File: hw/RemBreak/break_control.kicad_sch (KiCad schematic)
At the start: 13 parts, among them J6 Conn_01x07, J7 Conn_01x07, J8 Conn_01x03, Q10 BC337, Q11 BC847

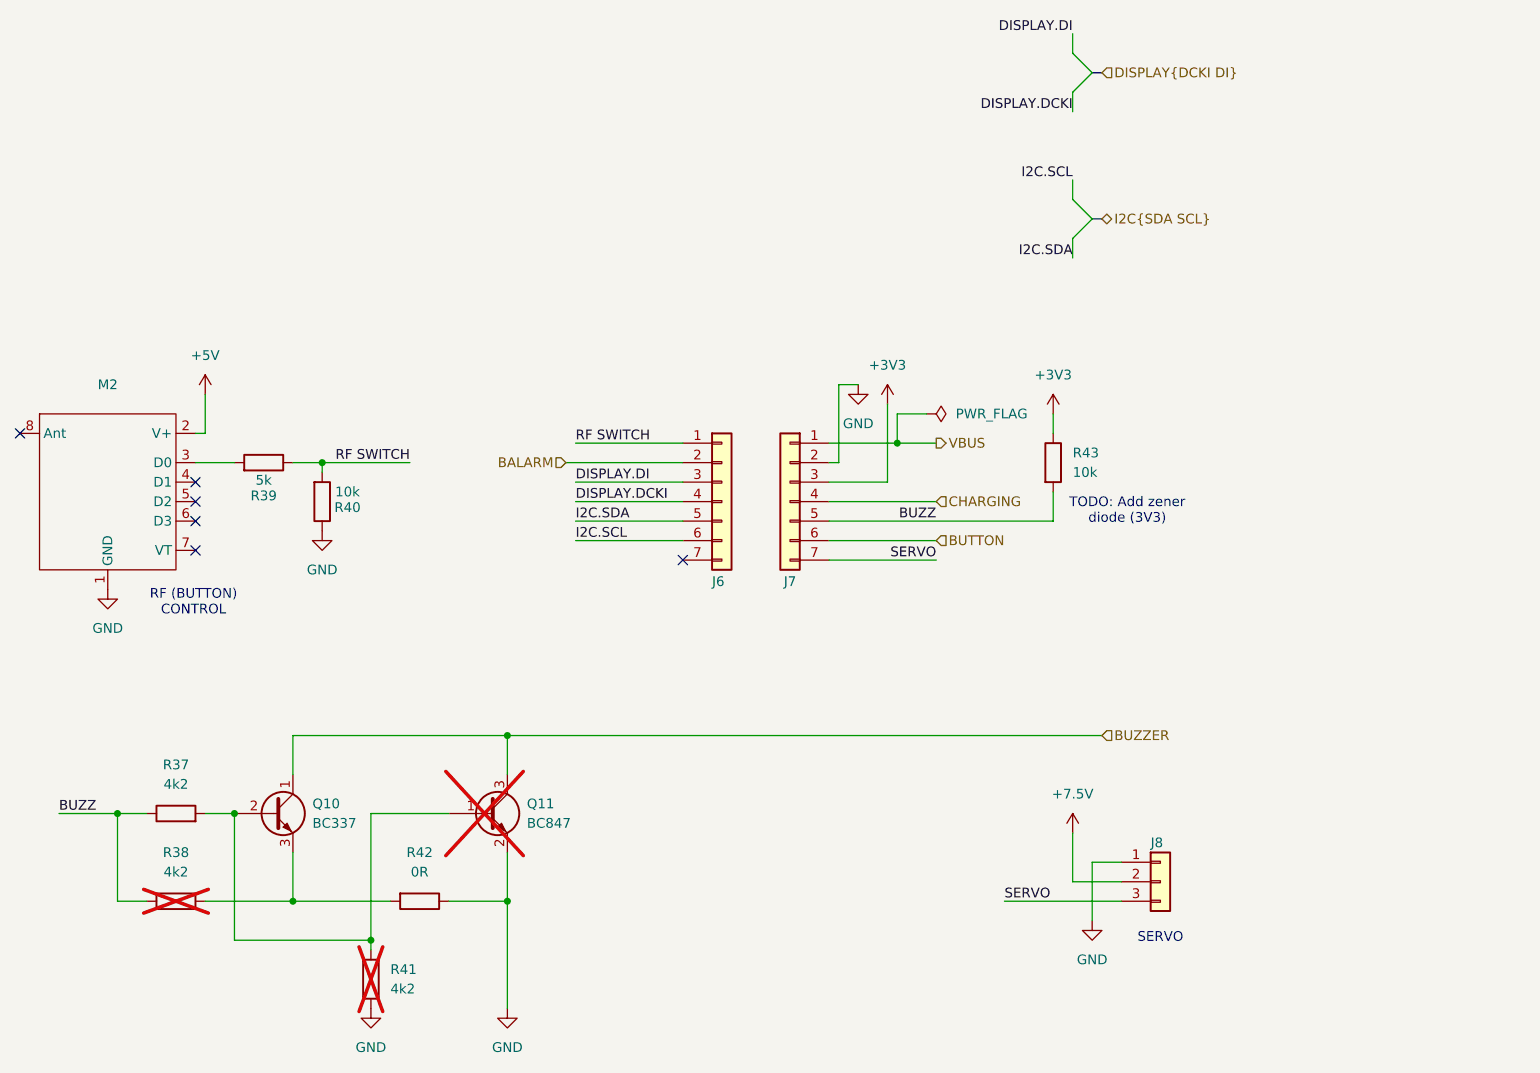
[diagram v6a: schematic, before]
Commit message: Note fonts changed to bold and added titles of the sheets included rev number
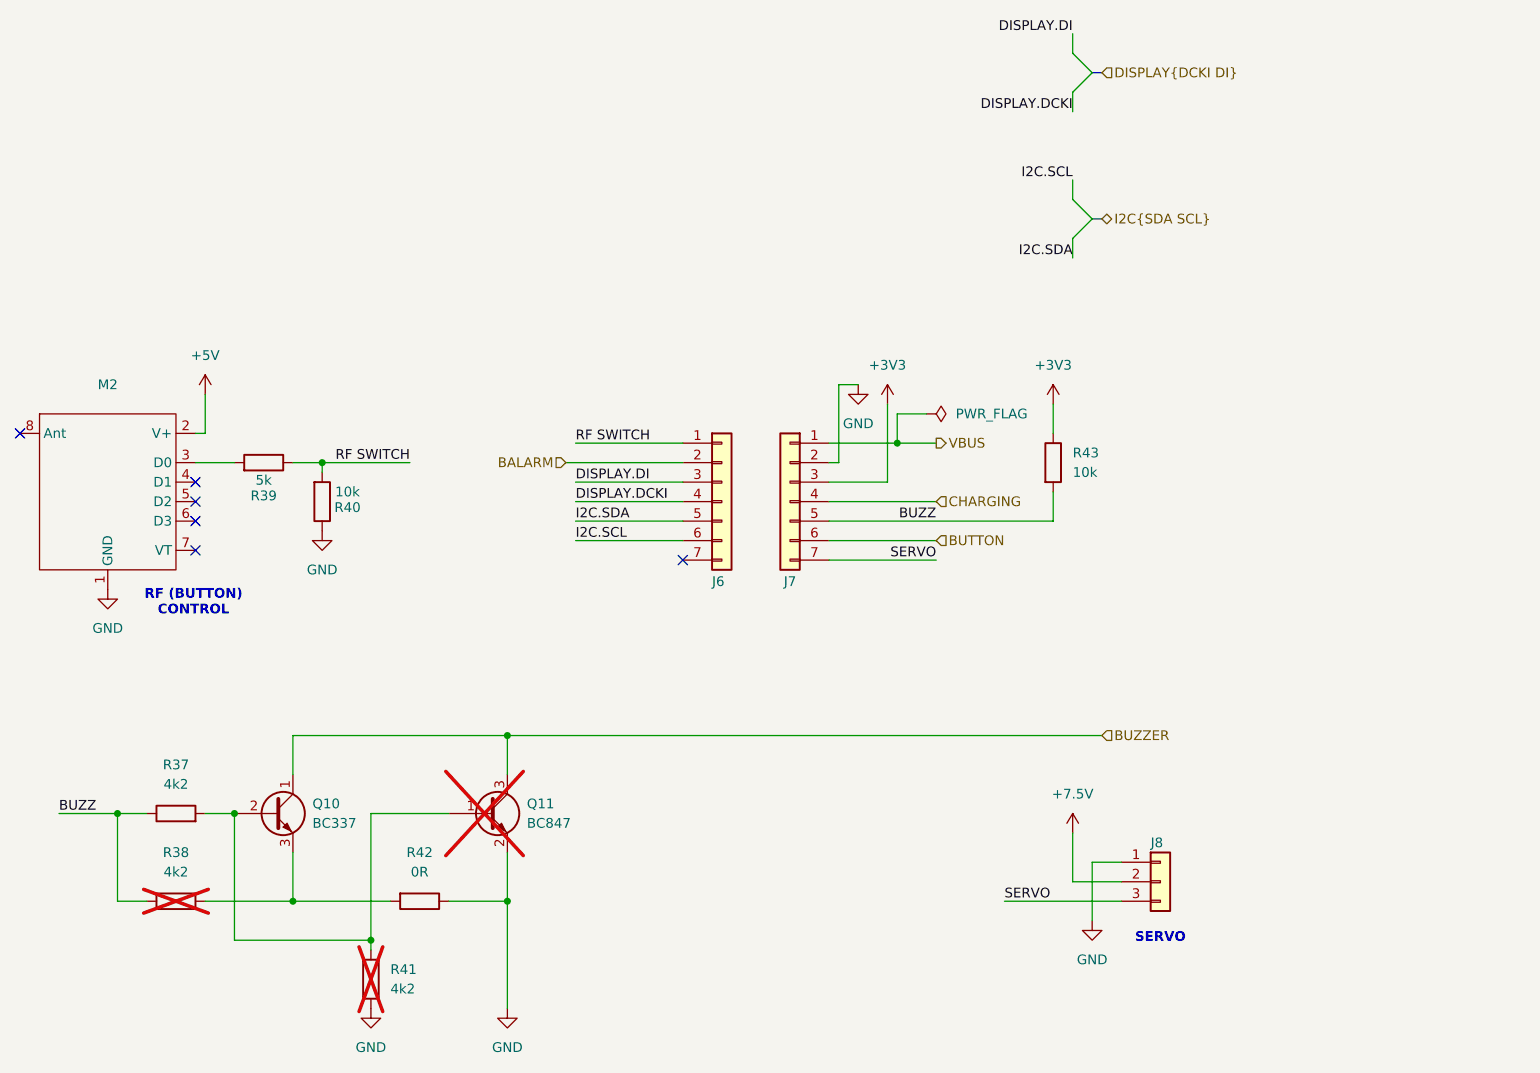
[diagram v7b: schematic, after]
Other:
- note removed: "TODO: Add zener diode (3V3)"
- title: (none) -> Break Control
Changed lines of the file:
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@@
 	(generator_version "8.99")
 	(paper "A4")
+	(title_block
+		(title "Break Control")
+		(date "2024-12-15")
+		(rev "1.0")
+	)
 	(bus_alias "DISPLAY"
 		(members "DISP_DI" "DISP_DCKI")
@@
 			(font
 				(size 1.27 1.27)
-			)
-		)
-	)
-	(text "TODO: Add zener \ndiode (3V3)"
-		(exclude_from_sim no)
-		(at 198.882 95.25 0)
-		(effects
-			(font
-				(size 1.27 1.27)
-				(color 255 0 0 1)
+				(thickness 0.254)
+				(bold yes)
 			)
 		)
@@
 			(font
 				(size 1.27 1.27)
+				(thickness 0.254)
+				(bold yes)
 			)
 		)
@@
 	(wire
 		(pts
-			(xy 189.23 82.55) (xy 189.23 85.09)
+			(xy 189.23 81.28) (xy 189.23 85.09)
 		)
 		(stroke
@@
 	(symbol
 		(lib_id "power:+3V3")
-		(at 189.23 82.55 0)
+		(at 189.23 81.28 0)
 		(unit 1)
 		(exclude_from_sim no)
@@
 		(fields_autoplaced yes)
 		(property "Reference" "#PWR045"
-			(at 189.23 86.36 0)
+			(at 189.23 85.09 0)
 			(effects
 				(font
@@
 		)
 		(property "Value" "+3V3"
-			(at 189.23 77.47 0)
+			(at 189.23 76.2 0)
 			(effects
 				(font
@@
 		)
 		(property "Footprint" ""
-			(at 189.23 82.55 0)
+			(at 189.23 81.28 0)
 			(effects
 				(font
@@
 		)
 		(property "Datasheet" ""
-			(at 189.23 82.55 0)
+			(at 189.23 81.28 0)
 			(effects
 				(font
@@
 		)
 		(property "Description" "Power symbol creates a global label with name \"+3V3\""
-			(at 189.23 82.55 0)
-			(effects
-				(font
+			(at 189.23 81.28 0)
+			(effects
+				(font
